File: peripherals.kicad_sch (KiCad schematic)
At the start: 46 parts, among them J12 PinHeader_2x5_P1.27mm_SMD, J13 PinHeader_2x5_P1.27mm_SMD, J14 PinHeader_2x5_P1.27mm_SMD, J15 PinHeader_2x5_P1.27mm_SMD, J16 PinHeader_2x5_P1.27mm_SMD, J20 PinHeader_2x5_P1.27mm_SMD, J6 PinHeader_2x10_P1.27mm_SMD_Sh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, J7 JST_SH_1x4_BM04B-SRSS-TB-LF-SN, J8 PinHeader_1x2_P1.27mm_Drill0.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, J9 PinHeader_2x5_P1.27mm_SMD_Shr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, Q2 DMG1012T-7, Q3 DMG1012T-7, Q4 DMG1012T-7, U1 TMP75AIDR, U2 AT24C04C_SOIC8

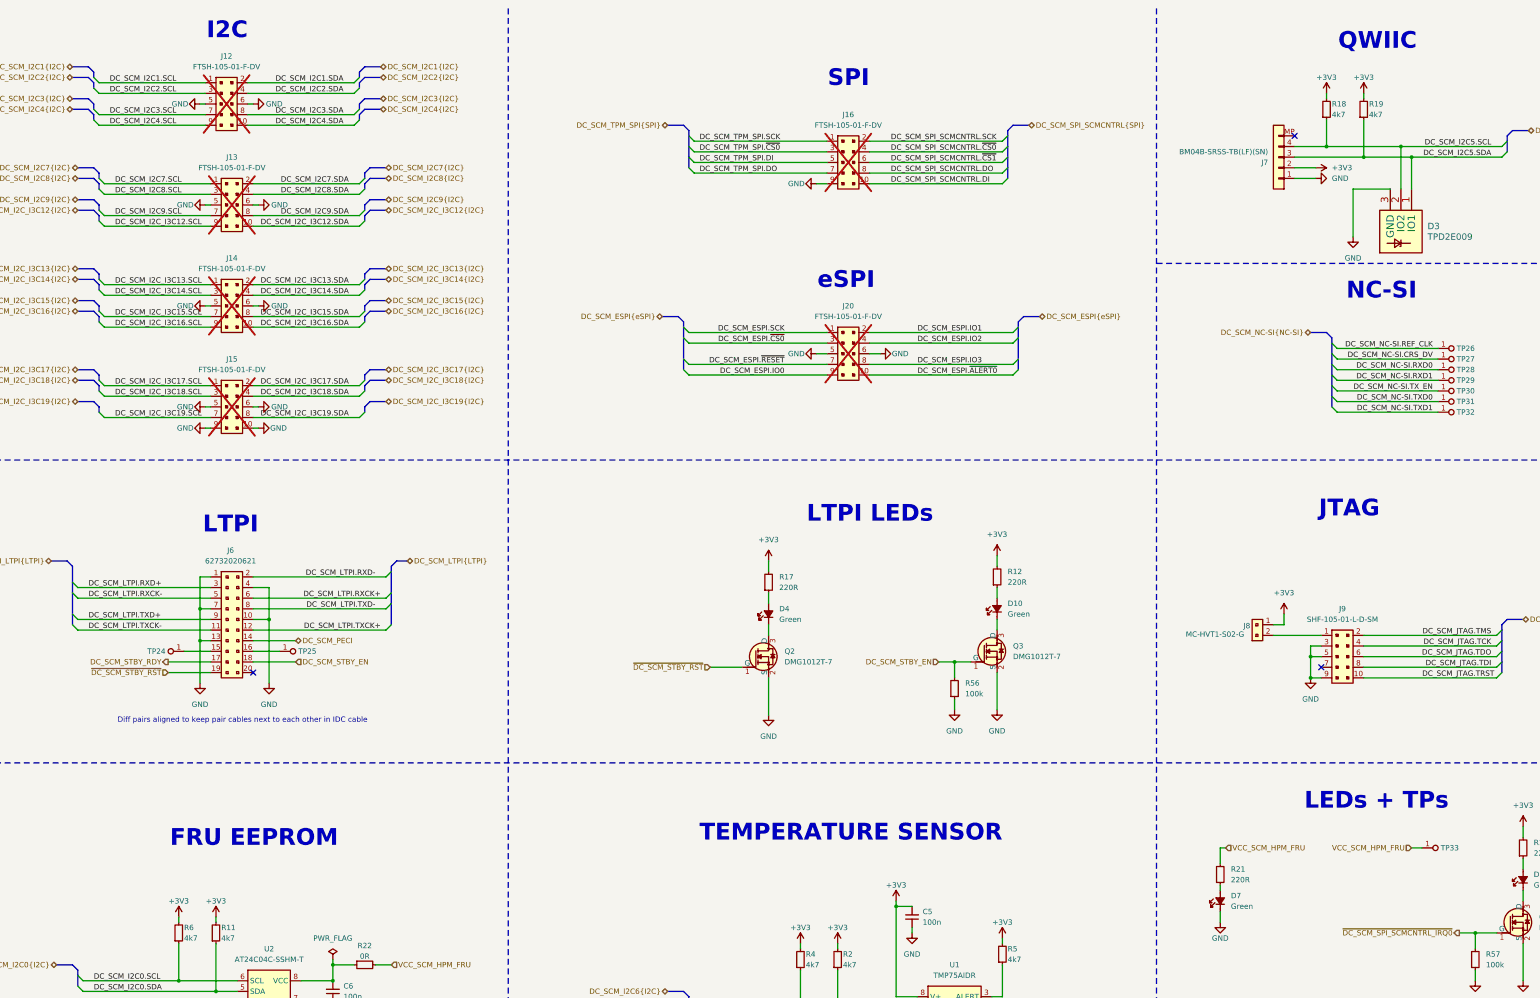
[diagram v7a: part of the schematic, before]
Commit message: [#93949] Change EEPROM pull-ups to VCC_SCM_HPM_FRU
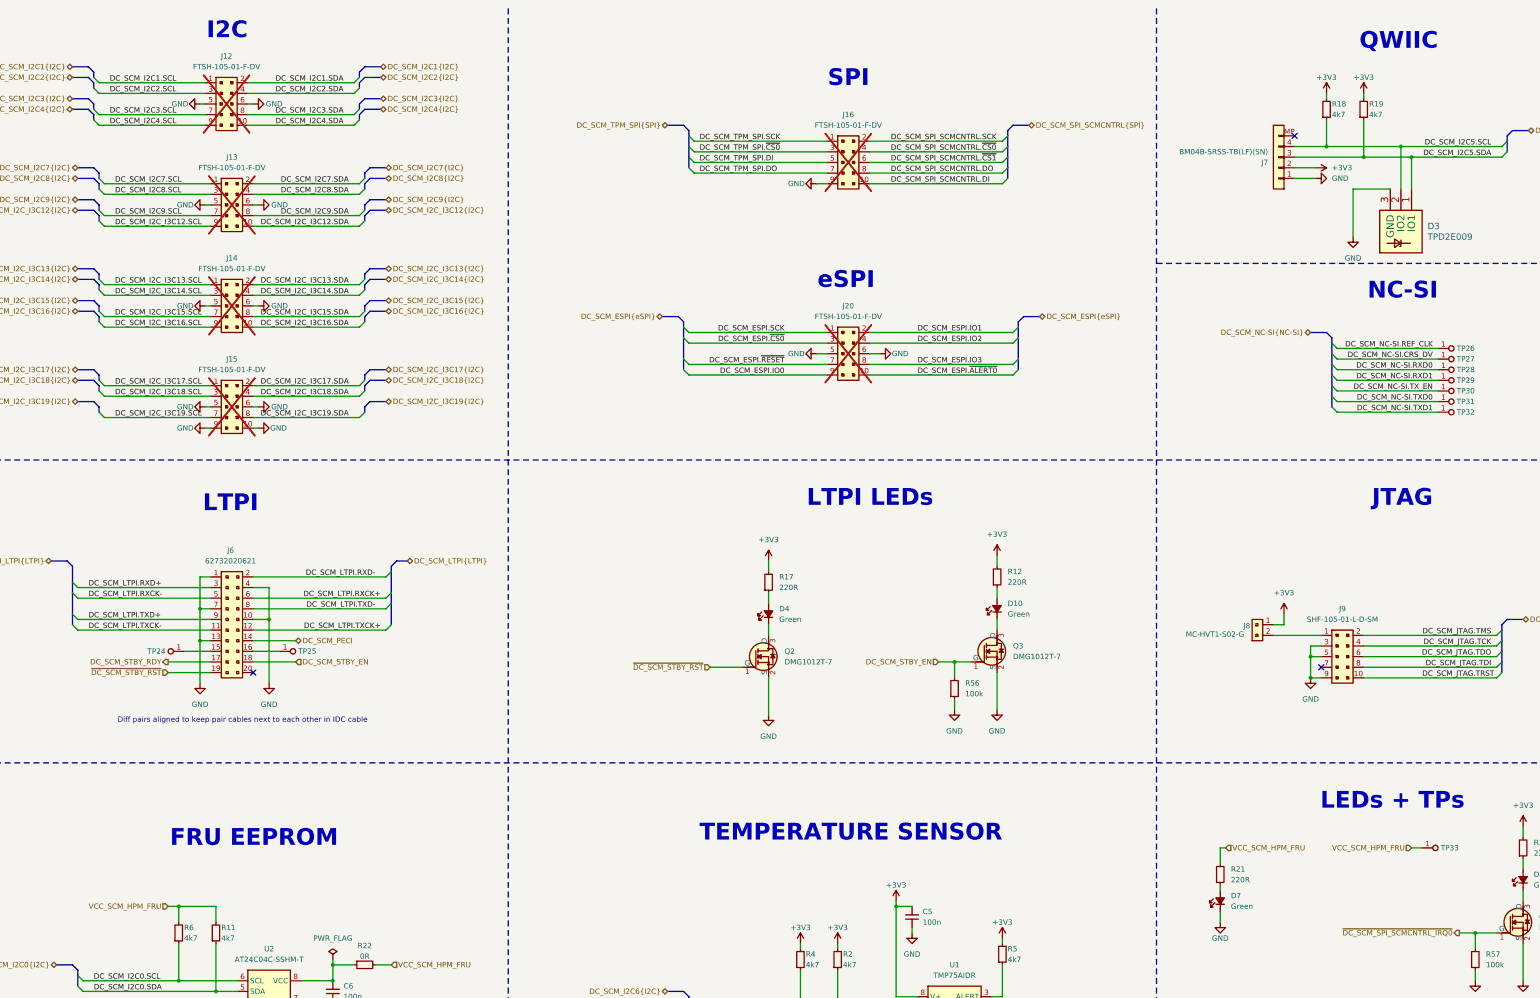
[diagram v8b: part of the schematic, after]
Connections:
- net +3V3: no longer R11.2, R6.2
- net VCC_SCM_HPM_FRU: now also R11.2, R6.2
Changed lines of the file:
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@@
 	(text "QWIIC"
 		(exclude_from_sim no)
-		(at 359.41 22.86 0)
+		(at 364.49 22.86 0)
 		(effects
 			(font
@@
 	(text "NC-SI\n"
 		(exclude_from_sim no)
-		(at 359.41 82.55 0)
+		(at 364.49 82.55 0)
 		(effects
 			(font
@@
 	(text "LEDs + TPs"
 		(exclude_from_sim no)
-		(at 367.03 204.47 0)
+		(at 370.84 204.47 0)
 		(effects
 			(font
@@
 	(text "LTPI\n"
 		(exclude_from_sim no)
-		(at 82.55 138.43 0)
+		(at 82.55 133.35 0)
 		(effects
 			(font
@@
 	(text "LTPI LEDs\n"
 		(exclude_from_sim no)
-		(at 243.84 135.89 0)
+		(at 243.84 132.08 0)
 		(effects
 			(font
@@
 	(text "JTAG\n"
 		(exclude_from_sim no)
-		(at 350.52 134.62 0)
+		(at 363.22 132.08 0)
 		(effects
 			(font
@@
 	)
 	(junction
+		(at 63.5 227.33)
+		(diameter 0)
+		(color 0 0 0 0)
+	)
+	(junction
 		(at 68.58 163.83)
 		(diameter 0)
@@
 		)
 	)
+	(wire
+		(pts
+			(xy 72.39 227.33) (xy 72.39 231.14)
+		)
+		(stroke
+			(width 0)
+			(type default)
+		)
+	)
 	(bus
 		(pts
@@
 	(wire
 		(pts
+			(xy 63.5 227.33) (xy 63.5 231.14)
+		)
+		(stroke
+			(width 0)
+			(type default)
+		)
+	)
+	(wire
+		(pts
 			(xy 100.33 241.3) (xy 105.41 241.3)
 		)
@@
 	(wire
 		(pts
-			(xy 72.39 229.87) (xy 72.39 231.14)
-		)
-		(stroke
-			(width 0)
-			(type default)
-		)
-	)
-	(wire
-		(pts
 			(xy 340.36 106.68) (xy 364.49 106.68)
 		)
@@
 	(wire
 		(pts
+			(xy 60.96 227.33) (xy 63.5 227.33)
+		)
+		(stroke
+			(width 0)
+			(type default)
+		)
+	)
+	(wire
+		(pts
 			(xy 259.08 171.45) (xy 259.08 180.34)
 		)
@@
 	(wire
 		(pts
-			(xy 63.5 229.87) (xy 63.5 231.14)
-		)
-		(stroke
-			(width 0)
-			(type default)
-		)
-	)
-	(wire
-		(pts
 			(xy 231.14 95.25) (xy 228.6 95.25)
 		)
@@
 		)
 	)
+	(wire
+		(pts
+			(xy 63.5 227.33) (xy 72.39 227.33)
+		)
+		(stroke
+			(width 0)
+			(type default)
+		)
+	)
 	(bus
 		(pts
@@
 		)
 	)
+	(hierarchical_label "VCC_SCM_HPM_FRU"
+		(shape input)
+		(at 60.96 227.33 180)
+		(effects
+			(font
+				(size 1.27 1.27)
+			)
+			(justify right)
+		)
+	)
 	(hierarchical_label "DC_SCM_I2C4{I2C}"
 		(shape bidirectional)
@@
 	)
 	(symbol
-		(lib_name "+3V3_1")
-		(lib_id "antmicropower:+3V3")
-		(at 72.39 229.87 0)
-		(unit 1)
-		(exclude_from_sim no)
-		(in_bom yes)
-		(on_board yes)
-		(dnp no)
-		(property "Reference" "#PWR018"
-			(at 87.63 229.87 0)
-			(effects
-				(font
-					(size 1.27 1.27)
-					(thickness 0.15)
-				)
-				(justify left bottom)
-				(hide yes)
-			)
-		)
-		(property "Value" "+3V3"
-			(at 72.39 226.06 0)
-			(effects
-				(font
-					(size 1.27 1.27)
-					(thickness 0.15)
-				)
-			)
-		)
-		(property "Footprint" ""
-			(at 87.63 237.49 0)
-			(effects
-				(font
-					(size 1.27 1.27)
-					(thickness 0.15)
-				)
-				(justify left bottom)
-				(hide yes)
-			)
-		)
-		(property "Datasheet" ""
-			(at 87.63 240.03 0)
-			(effects
-				(font
-					(size 1.27 1.27)
-					(thickness 0.15)
-				)
-				(justify left bottom)
-				(hide yes)
-			)
-		)
-		(property "Description" ""
-			(at 87.63 242.57 0)
-			(effects
-				(font
-					(size 1.27 1.27)
-				)
-				(justify left bottom)
-				(hide yes)
-			)
-		)
-		(property "Author" "Antmicro"
-			(at 87.63 232.41 0)
-			(effects
-				(font
-					(size 1.27 1.27)
-					(thickness 0.15)
-				)
-				(justify left bottom)
-				(hide yes)
-			)
-		)
-		(property "License" "Apache-2.0"
-			(at 87.63 234.95 0)
-			(effects
-				(font
-					(size 1.27 1.27)
-					(thickness 0.15)
-				)
-				(justify left bottom)
-				(hide yes)
-			)
-		)
-		(pin "1"
-		)
-		(instances
-			(project "bmc-breakout-board"
-				(path "/5d67ef28-5805-4f87-b722-2926dabf7f6e/f1ecdd24-c7ef-4765-8186-53d06f23944d"
-					(reference "#PWR018")
-					(unit 1)
-				)
-			)
-		)
-	)
-	(symbol
 		(lib_name "LED_G_0402_VLMTG1500-GS08_2")
 		(lib_id "antmicroLEDIndicationDiscrete:LED_G_0402_VLMTG1500-GS08")
@@
 					(unit 1)
 				)
-			)
-		)
-	)
-	(symbol
-		(lib_name "+3V3_1")
-		(lib_id "antmicropower:+3V3")
-		(at 63.5 229.87 0)
-		(unit 1)
-		(exclude_from_sim no)
-		(in_bom yes)
-		(on_board yes)
-		(dnp no)
-		(property "Reference" "#PWR017"
-			(at 78.74 229.87 0)
-			(effects
-				(font
-					(size 1.27 1.27)
-					(thickness 0.15)
-				)
-				(justify left bottom)
-				(hide yes)
-			)
-		)
-		(property "Value" "+3V3"
-			(at 63.5 226.06 0)
-			(effects
-				(font
-					(size 1.27 1.27)
-					(thickness 0.15)
-				)
-			)
-		)
-		(property "Footprint" ""
-			(at 78.74 237.49 0)
-			(effects
-				(font
-					(size 1.27 1.27)
-					(thickness 0.15)
-				)
-				(justify left bottom)
-				(hide yes)
-			)
-		)
-		(property "Datasheet" ""
-			(at 78.74 240.03 0)
-			(effects
-				(font
-					(size 1.27 1.27)
-					(thickness 0.15)
-				)
-				(justify left bottom)
-				(hide yes)
-			)
-		)
-		(property "Description" ""
-			(at 78.74 242.57 0)
-			(effects
-				(font
-					(size 1.27 1.27)
-				)
-				(justify left bottom)
-				(hide yes)
-			)
-		)
-		(property "Author" "Antmicro"
-			(at 78.74 232.41 0)
-			(effects
-				(font
-					(size 1.27 1.27)
-					(thickness 0.15)
-				)
-				(justify left bottom)
-				(hide yes)
-			)
-		)
-		(property "License" "Apache-2.0"
-			(at 78.74 234.95 0)
-			(effects
-				(font
-					(size 1.27 1.27)
-					(thickness 0.15)
-				)
-				(justify left bottom)
-				(hide yes)
-			)
-		)
-		(pin "1"
-		)
-		(instances
-			(project "bmc-breakout-board"
-				(path "/5d67ef28-5805-4f87-b722-2926dabf7f6e/f1ecdd24-c7ef-4765-8186-53d06f23944d"
-					(reference "#PWR017")
-					(unit 1)
-				)
